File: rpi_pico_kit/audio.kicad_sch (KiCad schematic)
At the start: 37 parts, among them J13 AudioJack-CUI-SJ-3523-SMT, J14 AudioJack-CUI-SJ-3523-SMT, Q7 DMN63D8L-7, U10 74LVC2G34GV, U11 PCM5101A, U9 NCP115-3.3_SOT23-5

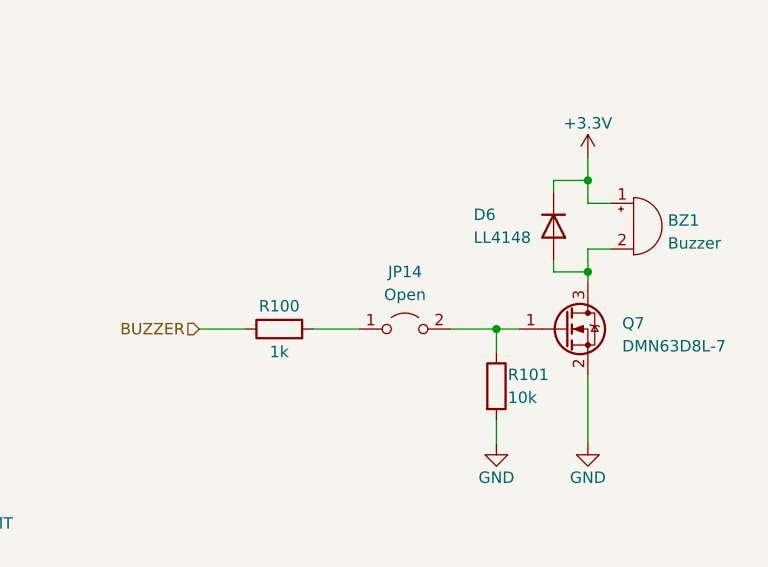
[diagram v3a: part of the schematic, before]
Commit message: added solder jumpers to swd, changed numbering of parts
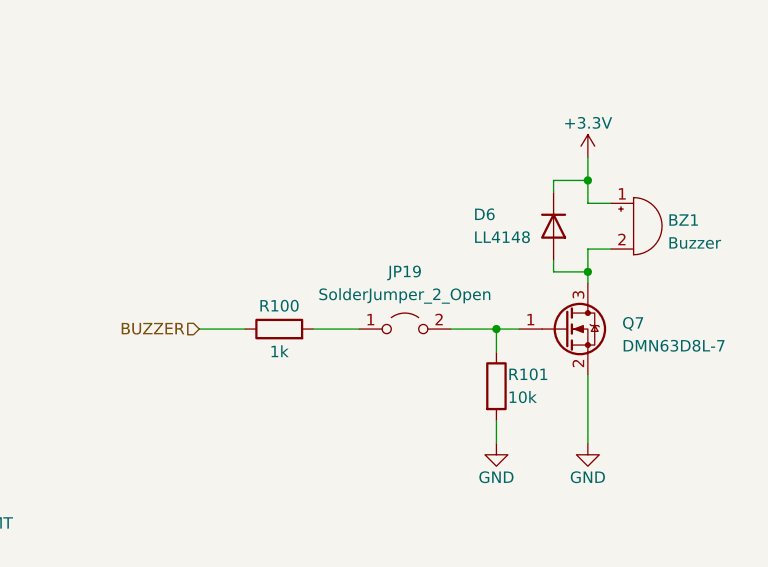
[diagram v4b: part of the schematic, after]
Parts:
- JP19: renamed from JP14; value Open -> SolderJumper_2_Open
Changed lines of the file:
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@@
   (symbol (lib_id "power:GND") (at 57.15 167.64 0) (unit 1)
     (in_bom yes) (on_board yes)
-    (property "Reference" "#PWR?" (id 0) (at 57.15 173.99 0)
+    (property "Reference" "#PWR0125" (id 0) (at 57.15 173.99 0)
       (effects (font (size 1.27 1.27)) hide)
     )
@@
   (symbol (lib_id "power:GND") (at 86.36 120.65 0) (unit 1)
     (in_bom yes) (on_board yes)
-    (property "Reference" "#PWR?" (id 0) (at 86.36 127 0)
+    (property "Reference" "#PWR0131" (id 0) (at 86.36 127 0)
       (effects (font (size 1.27 1.27)) hide)
     )
@@
   (symbol (lib_id "power:GND") (at 113.03 148.59 0) (unit 1)
     (in_bom yes) (on_board yes)
-    (property "Reference" "#PWR?" (id 0) (at 113.03 154.94 0)
+    (property "Reference" "#PWR0142" (id 0) (at 113.03 154.94 0)
       (effects (font (size 1.27 1.27)) hide)
     )
@@
   (symbol (lib_id "power:GND") (at 97.79 120.65 0) (unit 1)
     (in_bom yes) (on_board yes)
-    (property "Reference" "#PWR?" (id 0) (at 97.79 127 0)
+    (property "Reference" "#PWR0135" (id 0) (at 97.79 127 0)
       (effects (font (size 1.27 1.27)) hide)
     )
@@
   (symbol (lib_id "Jumper:Jumper_2_Open") (at 219.71 114.3 0) (unit 1)
     (in_bom yes) (on_board yes)
-    (property "Reference" "JP14" (id 0) (at 219.71 107.95 0)
-      (effects (font (size 1.27 1.27)))
-    )
-    (property "Value" "Open" (id 1) (at 219.71 110.49 0)
+    (property "Reference" "JP19" (id 0) (at 219.71 107.95 0)
+      (effects (font (size 1.27 1.27)))
+    )
+    (property "Value" "SolderJumper_2_Open" (id 1) (at 219.71 110.49 0)
       (effects (font (size 1.27 1.27)))
     )
@@
   (symbol (lib_id "power:GND") (at 124.46 120.65 0) (unit 1)
     (in_bom yes) (on_board yes)
-    (property "Reference" "#PWR?" (id 0) (at 124.46 127 0)
+    (property "Reference" "#PWR0143" (id 0) (at 124.46 127 0)
       (effects (font (size 1.27 1.27)) hide)
     )
@@
   (symbol (lib_id "power:GND") (at 125.73 57.15 0) (unit 1)
     (in_bom yes) (on_board yes)
-    (property "Reference" "#PWR?" (id 0) (at 125.73 63.5 0)
+    (property "Reference" "#PWR0145" (id 0) (at 125.73 63.5 0)
       (effects (font (size 1.27 1.27)) hide)
     )
@@
   (symbol (lib_id "power:+3.3V") (at 72.39 106.68 0) (unit 1)
     (in_bom yes) (on_board yes)
-    (property "Reference" "#PWR?" (id 0) (at 72.39 110.49 0)
+    (property "Reference" "#PWR0129" (id 0) (at 72.39 110.49 0)
       (effects (font (size 1.27 1.27)) hide)
     )
@@
   (symbol (lib_id "power:+5V") (at 210.82 55.88 0) (unit 1)
     (in_bom yes) (on_board yes)
-    (property "Reference" "#PWR?" (id 0) (at 210.82 59.69 0)
+    (property "Reference" "#PWR0147" (id 0) (at 210.82 59.69 0)
       (effects (font (size 1.27 1.27)) hide)
     )
@@
   (symbol (lib_id "power:GND") (at 58.42 120.65 0) (unit 1)
     (in_bom yes) (on_board yes)
-    (property "Reference" "#PWR?" (id 0) (at 58.42 127 0)
+    (property "Reference" "#PWR0126" (id 0) (at 58.42 127 0)
       (effects (font (size 1.27 1.27)) hide)
     )
@@
   (symbol (lib_id "power:GND") (at 87.63 167.64 0) (unit 1)
     (in_bom yes) (on_board yes)
-    (property "Reference" "#PWR?" (id 0) (at 87.63 173.99 0)
+    (property "Reference" "#PWR0132" (id 0) (at 87.63 173.99 0)
       (effects (font (size 1.27 1.27)) hide)
     )
@@
   (symbol (lib_id "power:GND") (at 72.39 167.64 0) (unit 1)
     (in_bom yes) (on_board yes)
-    (property "Reference" "#PWR?" (id 0) (at 72.39 173.99 0)
+    (property "Reference" "#PWR0130" (id 0) (at 72.39 173.99 0)
       (effects (font (size 1.27 1.27)) hide)
     )
@@
   (symbol (lib_id "power:GND") (at 46.99 120.65 0) (unit 1)
     (in_bom yes) (on_board yes)
-    (property "Reference" "#PWR?" (id 0) (at 46.99 127 0)
+    (property "Reference" "#PWR0123" (id 0) (at 46.99 127 0)
       (effects (font (size 1.27 1.27)) hide)
     )
@@
   (symbol (lib_id "power:GND") (at 243.84 71.12 0) (unit 1)
     (in_bom yes) (on_board yes)
-    (property "Reference" "#PWR?" (id 0) (at 243.84 77.47 0)
+    (property "Reference" "#PWR0154" (id 0) (at 243.84 77.47 0)
       (effects (font (size 1.27 1.27)) hide)
     )
@@
   (symbol (lib_id "power:GND") (at 137.16 139.7 0) (unit 1)
     (in_bom yes) (on_board yes)
-    (property "Reference" "#PWR?" (id 0) (at 137.16 146.05 0)
+    (property "Reference" "#PWR0146" (id 0) (at 137.16 146.05 0)
       (effects (font (size 1.27 1.27)) hide)
     )
@@
   (symbol (lib_id "power:+3.3V") (at 50.8 147.32 0) (unit 1)
     (in_bom yes) (on_board yes)
-    (property "Reference" "#PWR?" (id 0) (at 50.8 151.13 0)
+    (property "Reference" "#PWR0124" (id 0) (at 50.8 151.13 0)
       (effects (font (size 1.27 1.27)) hide)
     )
@@
   (symbol (lib_id "power:GND") (at 88.9 45.72 0) (unit 1)
     (in_bom yes) (on_board yes)
-    (property "Reference" "#PWR?" (id 0) (at 88.9 52.07 0)
+    (property "Reference" "#PWR0133" (id 0) (at 88.9 52.07 0)
       (effects (font (size 1.27 1.27)) hide)
     )
@@
   (symbol (lib_id "power:GND") (at 100.33 73.66 0) (unit 1)
     (in_bom yes) (on_board yes)
-    (property "Reference" "#PWR?" (id 0) (at 100.33 80.01 0)
+    (property "Reference" "#PWR0138" (id 0) (at 100.33 80.01 0)
       (effects (font (size 1.27 1.27)) hide)
     )
@@
   (symbol (lib_id "power:GND") (at 113.03 120.65 0) (unit 1)
     (in_bom yes) (on_board yes)
-    (property "Reference" "#PWR?" (id 0) (at 113.03 127 0)
+    (property "Reference" "#PWR0141" (id 0) (at 113.03 127 0)
       (effects (font (size 1.27 1.27)) hide)
     )
@@
   (symbol (lib_id "power:GND") (at 67.31 58.42 0) (unit 1)
     (in_bom yes) (on_board yes)
-    (property "Reference" "#PWR?" (id 0) (at 67.31 64.77 0)
+    (property "Reference" "#PWR0128" (id 0) (at 67.31 64.77 0)
       (effects (font (size 1.27 1.27)) hide)
     )
@@
   (symbol (lib_id "power:GND") (at 210.82 71.12 0) (unit 1)
     (in_bom yes) (on_board yes)
-    (property "Reference" "#PWR?" (id 0) (at 210.82 77.47 0)
+    (property "Reference" "#PWR0148" (id 0) (at 210.82 77.47 0)
       (effects (font (size 1.27 1.27)) hide)
     )
@@
   (symbol (lib_id "power:+3.3VA") (at 67.31 31.75 0) (unit 1)
     (in_bom yes) (on_board yes)
-    (property "Reference" "#PWR?" (id 0) (at 67.31 35.56 0)
+    (property "Reference" "#PWR0127" (id 0) (at 67.31 35.56 0)
       (effects (font (size 1.27 1.27)) hide)
     )
@@
   (symbol (lib_id "power:GND") (at 227.33 71.12 0) (unit 1)
     (in_bom yes) (on_board yes)
-    (property "Reference" "#PWR?" (id 0) (at 227.33 77.47 0)
+    (property "Reference" "#PWR0149" (id 0) (at 227.33 77.47 0)
       (effects (font (size 1.27 1.27)) hide)
     )
@@
   (symbol (lib_id "power:GND") (at 229.87 127 0) (unit 1)
     (in_bom yes) (on_board yes)
-    (property "Reference" "#PWR?" (id 0) (at 229.87 133.35 0)
+    (property "Reference" "#PWR0150" (id 0) (at 229.87 133.35 0)
       (effects (font (size 1.27 1.27)) hide)
     )
@@
   (symbol (lib_id "power:GND") (at 100.33 45.72 0) (unit 1)
     (in_bom yes) (on_board yes)
-    (property "Reference" "#PWR?" (id 0) (at 100.33 52.07 0)
+    (property "Reference" "#PWR0137" (id 0) (at 100.33 52.07 0)
       (effects (font (size 1.27 1.27)) hide)
     )
@@
   (symbol (lib_id "power:+3.3V") (at 240.03 95.25 0) (unit 1)
     (in_bom yes) (on_board yes)
-    (property "Reference" "#PWR?" (id 0) (at 240.03 99.06 0)
+    (property "Reference" "#PWR0151" (id 0) (at 240.03 99.06 0)
       (effects (font (size 1.27 1.27)) hide)
     )
@@
   (symbol (lib_id "power:GND") (at 113.03 45.72 0) (unit 1)
     (in_bom yes) (on_board yes)
-    (property "Reference" "#PWR?" (id 0) (at 113.03 52.07 0)
+    (property "Reference" "#PWR0139" (id 0) (at 113.03 52.07 0)
       (effects (font (size 1.27 1.27)) hide)
     )
@@
   (symbol (lib_id "power:+3.3VA") (at 243.84 55.88 0) (unit 1)
     (in_bom yes) (on_board yes)
-    (property "Reference" "#PWR?" (id 0) (at 243.84 59.69 0)
+    (property "Reference" "#PWR0153" (id 0) (at 243.84 59.69 0)
       (effects (font (size 1.27 1.27)) hide)
     )
@@
   (symbol (lib_id "power:GND") (at 41.91 45.72 0) (unit 1)
     (in_bom yes) (on_board yes)
-    (property "Reference" "#PWR?" (id 0) (at 41.91 52.07 0)
+    (property "Reference" "#PWR0121" (id 0) (at 41.91 52.07 0)
       (effects (font (size 1.27 1.27)) hide)
     )
@@
   (symbol (lib_id "power:GND") (at 113.03 73.66 0) (unit 1)
     (in_bom yes) (on_board yes)
-    (property "Reference" "#PWR?" (id 0) (at 113.03 80.01 0)
+    (property "Reference" "#PWR0140" (id 0) (at 113.03 80.01 0)
       (effects (font (size 1.27 1.27)) hide)
     )
@@
   (symbol (lib_id "power:GND") (at 88.9 73.66 0) (unit 1)
     (in_bom yes) (on_board yes)
-    (property "Reference" "#PWR?" (id 0) (at 88.9 80.01 0)
+    (property "Reference" "#PWR0134" (id 0) (at 88.9 80.01 0)
       (effects (font (size 1.27 1.27)) hide)
     )
@@
   (symbol (lib_id "power:GND") (at 124.46 148.59 0) (unit 1)
     (in_bom yes) (on_board yes)
-    (property "Reference" "#PWR?" (id 0) (at 124.46 154.94 0)
+    (property "Reference" "#PWR0144" (id 0) (at 124.46 154.94 0)
       (effects (font (size 1.27 1.27)) hide)
     )
@@
   (symbol (lib_id "power:GND") (at 240.03 127 0) (unit 1)
     (in_bom yes) (on_board yes)
-    (property "Reference" "#PWR?" (id 0) (at 240.03 133.35 0)
+    (property "Reference" "#PWR0152" (id 0) (at 240.03 133.35 0)
       (effects (font (size 1.27 1.27)) hide)
     )
@@
   (symbol (lib_id "power:+3.3VA") (at 46.99 106.68 0) (unit 1)
     (in_bom yes) (on_board yes)
-    (property "Reference" "#PWR?" (id 0) (at 46.99 110.49 0)
+    (property "Reference" "#PWR0122" (id 0) (at 46.99 110.49 0)
       (effects (font (size 1.27 1.27)) hide)
     )
@@
   (symbol (lib_id "power:GND") (at 99.06 167.64 0) (unit 1)
     (in_bom yes) (on_board yes)
-    (property "Reference" "#PWR?" (id 0) (at 99.06 173.99 0)
-      (effects (font (size 1.27 1.27)) hide)
-    )
+    (property "Reference" "#PWR0136" (id 0) (at 99.06 173.99 0)
+      (effects (font (size 1.27 1.27)) hide)
+    )
